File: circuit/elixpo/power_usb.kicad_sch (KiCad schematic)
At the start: 19 parts, among them J1 USB-C USB2 device, J2 LiPo JST-PH 3-pin, SW3 MAIN POWER, U3 USBLC6-2SC6, U4 BQ24074RGT, U5 TPS63031 3V3

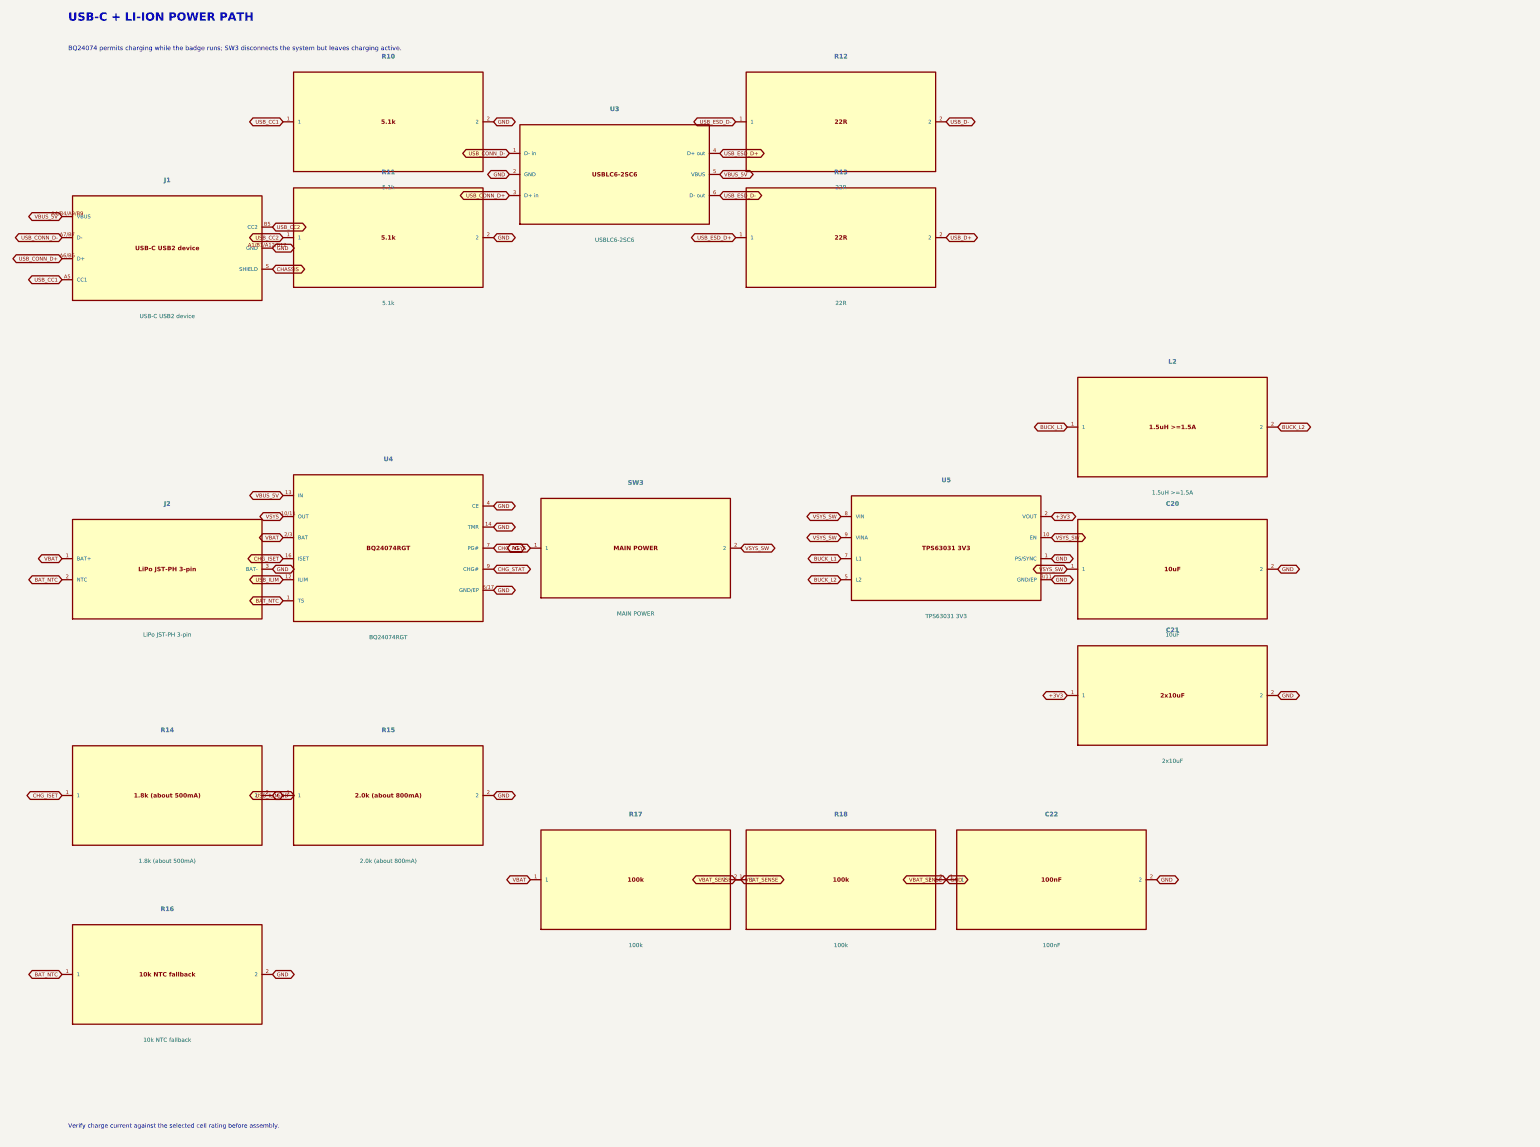
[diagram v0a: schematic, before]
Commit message: feat(hardware): complete badge schematic and procurement BOM
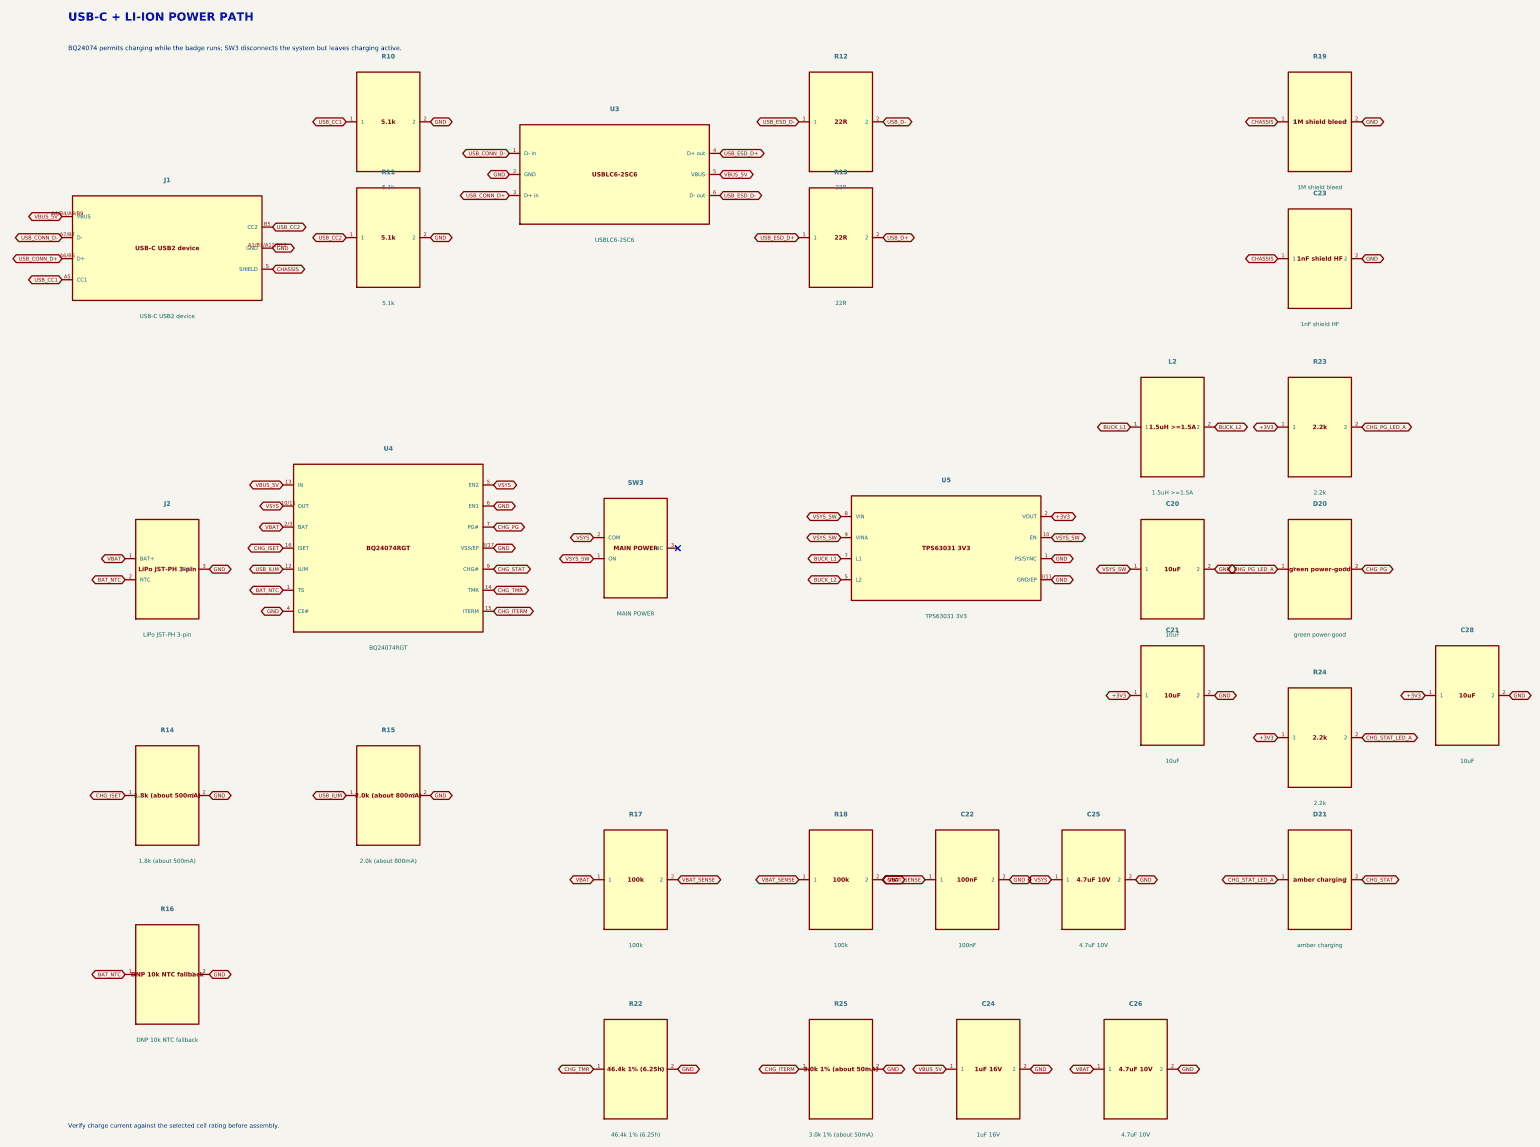
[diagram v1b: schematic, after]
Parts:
- added C23: 1nF shield HF, Capacitor_SMD:C_0402_1005Metric, symbol oreo_badge:C23
- added C24: 1uF 16V, Capacitor_SMD:C_0603_1608Metric, symbol oreo_badge:C24
- added C25: 4.7uF 10V, Capacitor_SMD:C_0603_1608Metric, symbol oreo_badge:C25
- added C26: 4.7uF 10V, Capacitor_SMD:C_0603_1608Metric, symbol oreo_badge:C26
- added C28: 10uF, Capacitor_SMD:C_0805_2012Metric, symbol oreo_badge:C28
- added D20: green power-good, LED_SMD:LED_0603_1608Metric, symbol oreo_badge:D20
- added D21: amber charging, LED_SMD:LED_0603_1608Metric, symbol oreo_badge:D21
- added R19: 1M shield bleed, Resistor_SMD:R_0402_1005Metric, symbol oreo_badge:R19
- added R22: 46.4k 1% (6.25h), Resistor_SMD:R_0402_1005Metric, symbol oreo_badge:R22
- added R23: 2.2k, Resistor_SMD:R_0402_1005Metric, symbol oreo_badge:R23
- added R24: 2.2k, Resistor_SMD:R_0402_1005Metric, symbol oreo_badge:R24
- added R25: 3.0k 1% (about 50mA), Resistor_SMD:R_0402_1005Metric, symbol oreo_badge:R25
- C21: value 2x10uF -> 10uF
- R16: value 10k NTC fallback -> DNP 10k NTC fallback
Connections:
- net +3V3: now also C28.1, R23.1, R24.1
- net CHASSIS: now also C23.1, R19.1
- net CHG_PG: now also D20.2
- net CHG_STAT: now also D21.2
- net GND: now also U4.6 (EN1), U4.8/17 (VSS/EP), C23.2, C24.2, C25.2, C26.2, C28.2, R19.2, R22.2, R25.2; no longer C22.1, R17.2, R18.1, U4.14 (TMR), U4.6/17 (GND/EP)
- net VBAT: now also C26.1
- net VBUS_5V: now also C24.1
- net VSYS: now also SW3.2 (COM), U4.5 (EN2), C25.1; no longer SW3.1
- net VSYS_SW: now also SW3.1 (ON); no longer SW3.2
- new net CHG_ITERM: R25.1, U4.15 (ITERM)
- new net CHG_PG_LED_A: D20.1, R23.2
- new net CHG_STAT_LED_A: D21.1, R24.2
- new net CHG_TMR: R22.1, U4.14 (TMR)
- new net VBAT_SENSE: C22.1, R17.2, R18.1
- no-connect marks 0 -> 1
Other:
- moved on the sheet: C22
